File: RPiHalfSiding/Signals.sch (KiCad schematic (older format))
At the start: 10 parts, among them J1 Address, T1 Signals A, B, T2 Signals C, D, U1 MCP23017, U2 ULN2803A, U3 ULN2803A

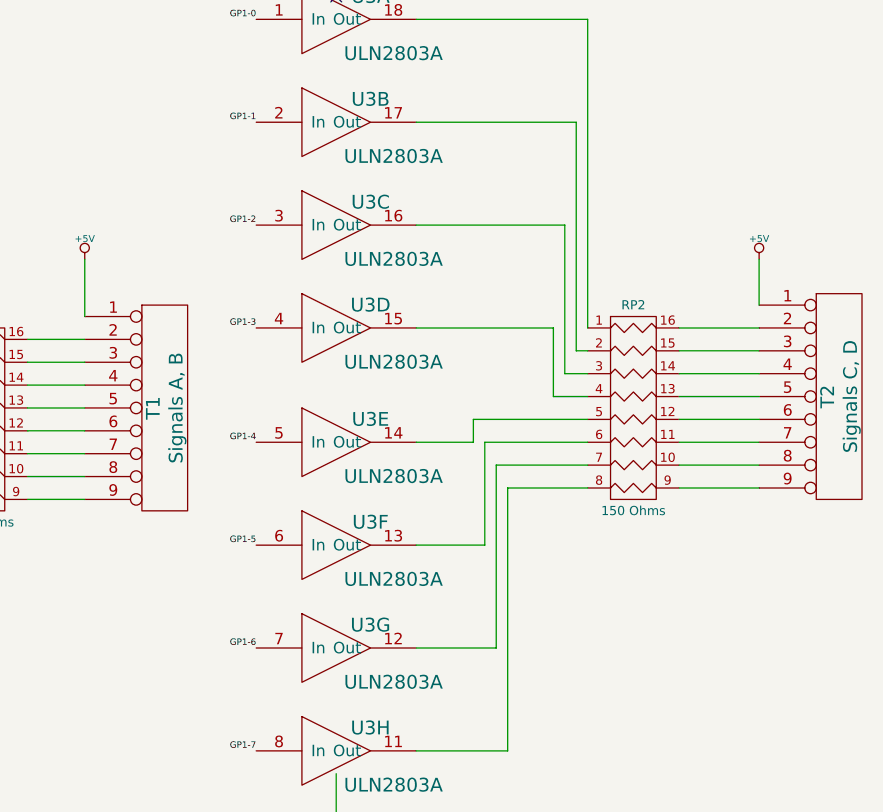
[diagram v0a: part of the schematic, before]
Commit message: Final Silktweaks for RPiHalfSiding
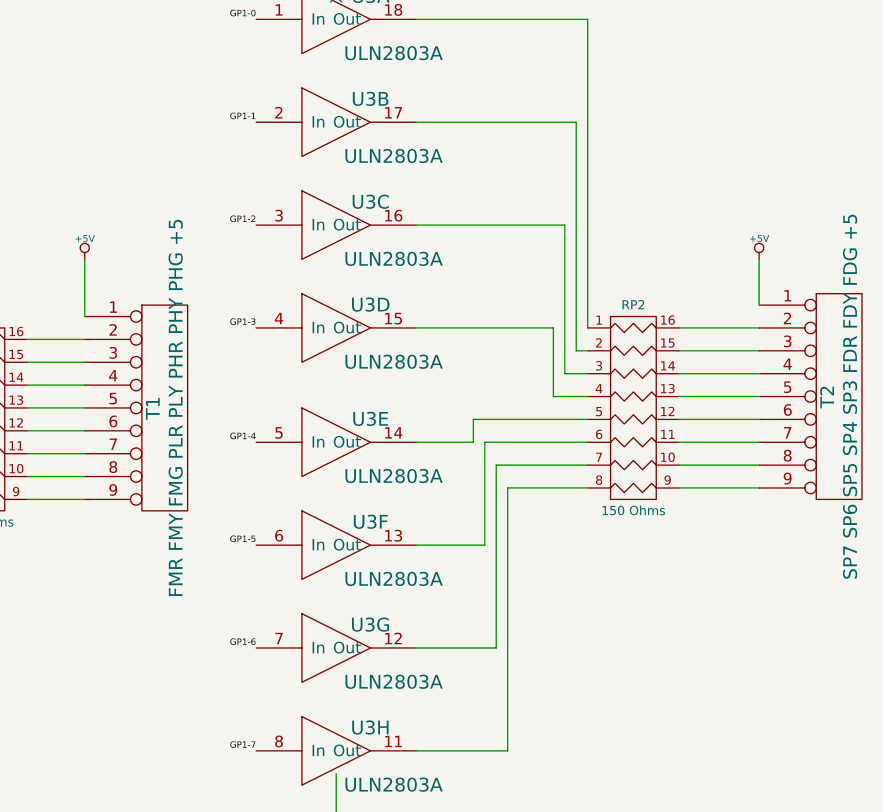
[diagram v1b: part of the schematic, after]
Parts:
- T1: value Signals A, B -> FMR FMY FMG PLR PLY PHR PHY PHG +5
- T2: value Signals C, D -> SP7 SP6 SP5 SP4 SP3 FDR FDY FDG +5
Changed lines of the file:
@@
 Sheet 2 3
 Title ""
-Date "8 oct 2018"
+Date "20 oct 2018"
 Rev ""
 Comp ""
@@
 P 7500 3800
 F 0 "T1" V 7450 3800 60  0000 C CNN
-F 1 "Signals A, B" V 7550 3800 60  0000 C CNN
+F 1 "FMR FMY FMG PLR PLY PHR PHY PHG +5" V 7550 3800 60  0000 C CNN
 F 2 "~" H 7500 3800 60  0000 C CNN
 F 3 "~" H 7500 3800 60  0000 C CNN
@@
 P 10450 3750
 F 0 "T2" V 10400 3750 60  0000 C CNN
-F 1 "Signals C, D" V 10500 3750 60  0000 C CNN
+F 1 "SP7 SP6 SP5 SP4 SP3 FDR FDY FDG +5" V 10500 3750 60  0000 C CNN
 F 2 "~" H 10450 3750 60  0000 C CNN
 F 3 "~" H 10450 3750 60  0000 C CNN
